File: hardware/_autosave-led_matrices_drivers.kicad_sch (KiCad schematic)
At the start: 12 parts, among them U6 MAX7219, U7 MAX7219, U8 MAX7219, U9 MAX7219

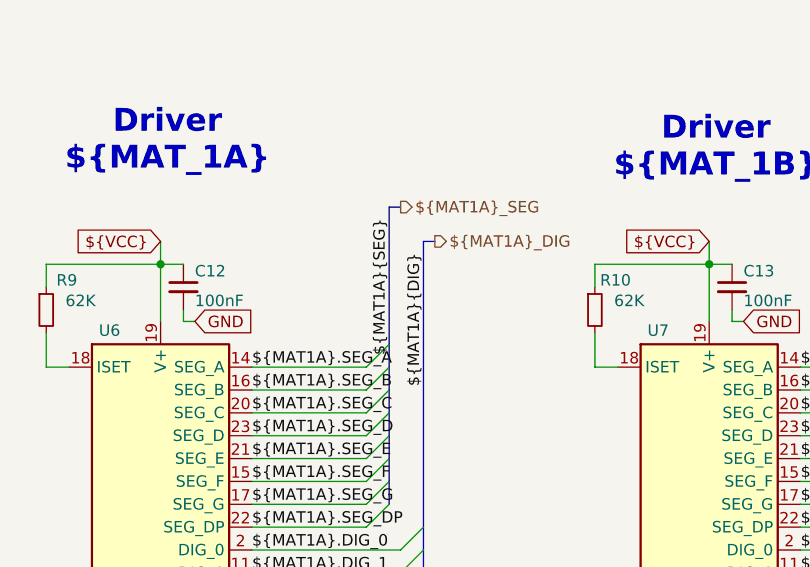
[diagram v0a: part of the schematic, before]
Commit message: Made some small changes on the properties of some components while having last weeks meeting and added the fp-info-cache to the gitignore file
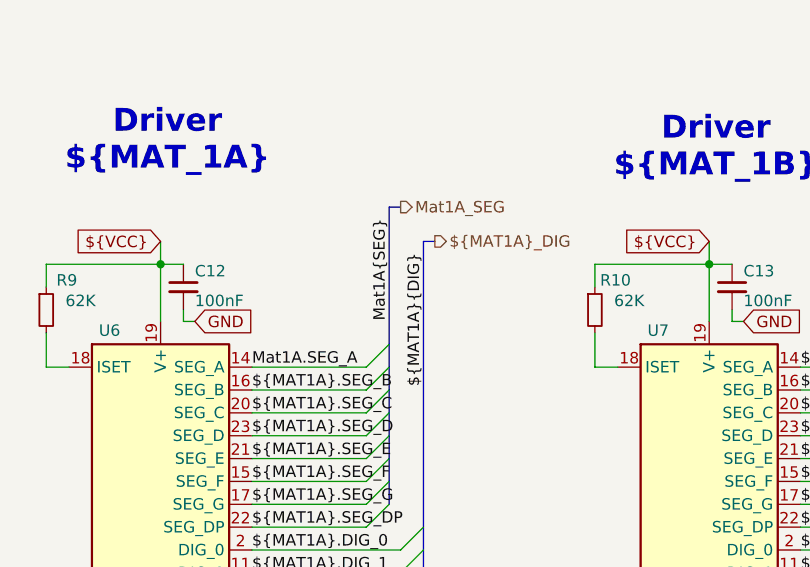
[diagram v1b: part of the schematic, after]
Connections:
- net ${MAT1A}.SEG_A renamed Mat1A.SEG_A
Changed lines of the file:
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@@
+	(bus
+		(pts
+			(xy 72.39 55.88) (xy 72.39 71.12)
+		)
+		(stroke
+			(width 0)
+			(type default)
+		)
+	)
+	(wire
+		(pts
+			(xy 69.85 73.66) (xy 57.15 73.66)
+		)
+		(stroke
+			(width 0)
+			(type default)
+		)
+	)
+	(bus
+		(pts
+			(xy 77.47 59.69) (xy 76.2 59.69)
+		)
+		(stroke
+			(width 0)
+			(type default)
+		)
+	)
+	(wire
+		(pts
+			(xy 154.94 69.85) (xy 154.94 73.66)
+		)
+		(stroke
+			(width 0)
+			(type default)
+		)
+	)
+	(bus
+		(pts
+			(xy 138.43 104.14) (xy 138.43 106.68)
+		)
+		(stroke
+			(width 0)
+			(type default)
+		)
+	)
+	(wire
+		(pts
+			(xy 240.03 78.74) (xy 254 78.74)
+		)
+		(stroke
+			(width 0)
+			(type default)
+		)
+	)
+	(wire
+		(pts
+			(xy 177.8 99.06) (xy 194.31 99.06)
+		)
+		(stroke
+			(width 0)
+			(type default)
+		)
+	)
+	(wire
+		(pts
+			(xy 118.11 111.76) (xy 135.89 111.76)
+		)
+		(stroke
+			(width 0)
+			(type default)
+		)
+	)
+	(bus
+		(pts
+			(xy 139.7 59.69) (xy 138.43 59.69)
+		)
+		(stroke
+			(width 0)
+			(type default)
+		)
+	)
+	(bus
+		(pts
+			(xy 256.54 86.36) (xy 256.54 88.9)
+		)
+		(stroke
+			(width 0)
+			(type default)
+		)
+	)
+	(bus
+		(pts
+			(xy 193.04 73.66) (xy 193.04 76.2)
+		)
+		(stroke
+			(width 0)
+			(type default)
+		)
+	)
+	(bus
+		(pts
+			(xy 196.85 99.06) (xy 196.85 101.6)
+		)
+		(stroke
+			(width 0)
+			(type default)
+		)
+	)
+	(wire
+		(pts
+			(xy 57.15 78.74) (xy 69.85 78.74)
+		)
+		(stroke
+			(width 0)
+			(type default)
+		)
+	)
+	(wire
+		(pts
+			(xy 57.15 109.22) (xy 73.66 109.22)
+		)
+		(stroke
+			(width 0)
+			(type default)
+		)
+	)
+	(wire
+		(pts
+			(xy 57.15 101.6) (xy 73.66 101.6)
+		)
+		(stroke
+			(width 0)
+			(type default)
+		)
+	)
+	(wire
+		(pts
+			(xy 190.5 86.36) (xy 177.8 86.36)
+		)
+		(stroke
+			(width 0)
+			(type default)
+		)
+	)
+	(bus
+		(pts
+			(xy 256.54 55.88) (xy 256.54 71.12)
+		)
+		(stroke
+			(width 0)
+			(type default)
+		)
+	)
+	(wire
+		(pts
+			(xy 34.29 73.66) (xy 36.83 73.66)
+		)
+		(stroke
+			(width 0)
+			(type default)
+		)
+	)
+	(bus
+		(pts
+			(xy 193.04 83.82) (xy 193.04 86.36)
+		)
+		(stroke
+			(width 0)
+			(type default)
+		)
+	)
 	(bus
 		(pts
@@
 		)
 	)
-	(bus
-		(pts
-			(xy 77.47 59.69) (xy 76.2 59.69)
-		)
-		(stroke
-			(width 0)
-			(type default)
-		)
-	)
-	(wire
-		(pts
-			(xy 154.94 69.85) (xy 154.94 73.66)
-		)
-		(stroke
-			(width 0)
-			(type default)
-		)
-	)
-	(bus
-		(pts
-			(xy 138.43 104.14) (xy 138.43 106.68)
-		)
-		(stroke
-			(width 0)
-			(type default)
-		)
-	)
-	(wire
-		(pts
-			(xy 240.03 78.74) (xy 254 78.74)
-		)
-		(stroke
-			(width 0)
-			(type default)
-		)
-	)
-	(wire
-		(pts
-			(xy 177.8 99.06) (xy 194.31 99.06)
-		)
-		(stroke
-			(width 0)
-			(type default)
-		)
-	)
-	(wire
-		(pts
-			(xy 118.11 111.76) (xy 135.89 111.76)
-		)
-		(stroke
-			(width 0)
-			(type default)
-		)
-	)
-	(bus
-		(pts
-			(xy 139.7 59.69) (xy 138.43 59.69)
-		)
-		(stroke
-			(width 0)
-			(type default)
-		)
-	)
-	(bus
-		(pts
-			(xy 256.54 86.36) (xy 256.54 88.9)
-		)
-		(stroke
-			(width 0)
-			(type default)
-		)
-	)
-	(bus
-		(pts
-			(xy 193.04 73.66) (xy 193.04 76.2)
-		)
-		(stroke
-			(width 0)
-			(type default)
-		)
-	)
-	(bus
-		(pts
-			(xy 196.85 99.06) (xy 196.85 101.6)
-		)
-		(stroke
-			(width 0)
-			(type default)
-		)
-	)
-	(wire
-		(pts
-			(xy 57.15 78.74) (xy 69.85 78.74)
-		)
-		(stroke
-			(width 0)
-			(type default)
-		)
-	)
-	(wire
-		(pts
-			(xy 57.15 109.22) (xy 73.66 109.22)
-		)
-		(stroke
-			(width 0)
-			(type default)
-		)
-	)
-	(wire
-		(pts
-			(xy 57.15 101.6) (xy 73.66 101.6)
-		)
-		(stroke
-			(width 0)
-			(type default)
-		)
-	)
-	(wire
-		(pts
-			(xy 190.5 86.36) (xy 177.8 86.36)
-		)
-		(stroke
-			(width 0)
-			(type default)
-		)
-	)
-	(bus
-		(pts
-			(xy 256.54 55.88) (xy 256.54 71.12)
-		)
-		(stroke
-			(width 0)
-			(type default)
-		)
-	)
-	(wire
-		(pts
-			(xy 34.29 73.66) (xy 36.83 73.66)
-		)
-		(stroke
-			(width 0)
-			(type default)
-		)
-	)
-	(wire
-		(pts
-			(xy 69.85 73.66) (xy 57.15 73.66)
-		)
-		(stroke
-			(width 0)
-			(type default)
-		)
-	)
-	(bus
-		(pts
-			(xy 193.04 83.82) (xy 193.04 86.36)
-		)
-		(stroke
-			(width 0)
-			(type default)
-		)
-	)
 	(wire
 		(pts
@@
 		)
 	)
-	(bus
-		(pts
-			(xy 72.39 55.88) (xy 72.39 71.12)
-		)
-		(stroke
-			(width 0)
-			(type default)
-		)
-	)
 	(wire
 		(pts
@@
 	(bus
 		(pts
-			(xy 73.66 55.88) (xy 72.39 55.88)
+			(xy 72.39 55.88) (xy 73.66 55.88)
 		)
 		(stroke
@@
 		)
 	)
-	(label "${MAT1A}.SEG_A"
-		(at 57.15 73.66 0)
-		(effects
-			(font
-				(size 1.27 1.27)
-			)
-			(justify left bottom)
-		)
-	)
 	(label "${MAT1B}.SEG_C"
 		(at 118.11 78.74 0)
@@
 		)
 	)
-	(label "${MAT1A}{SEG}"
+	(label "Mat1A{SEG}"
 		(at 72.39 57.15 270)
 		(effects
@@
 	(label "${MAT2B}.SEG_C"
 		(at 240.03 78.74 0)
+		(effects
+			(font
+				(size 1.27 1.27)
+			)
+			(justify left bottom)
+		)
+	)
+	(label "Mat1A.SEG_A"
+		(at 57.15 73.66 0)
 		(effects
 			(font
@@
 		)
 	)
-	(hierarchical_label "${MAT1A}_SEG"
+	(hierarchical_label "Mat1A_SEG"
 		(shape output)
 		(at 73.66 55.88 0)
